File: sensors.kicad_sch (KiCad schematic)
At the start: 28 parts, among them IC1 TCA9548ARGERQ1, IC4 SGP40-D-R4, IC5 SGP40-D-R4, U2 BMP581, U4 BMP581

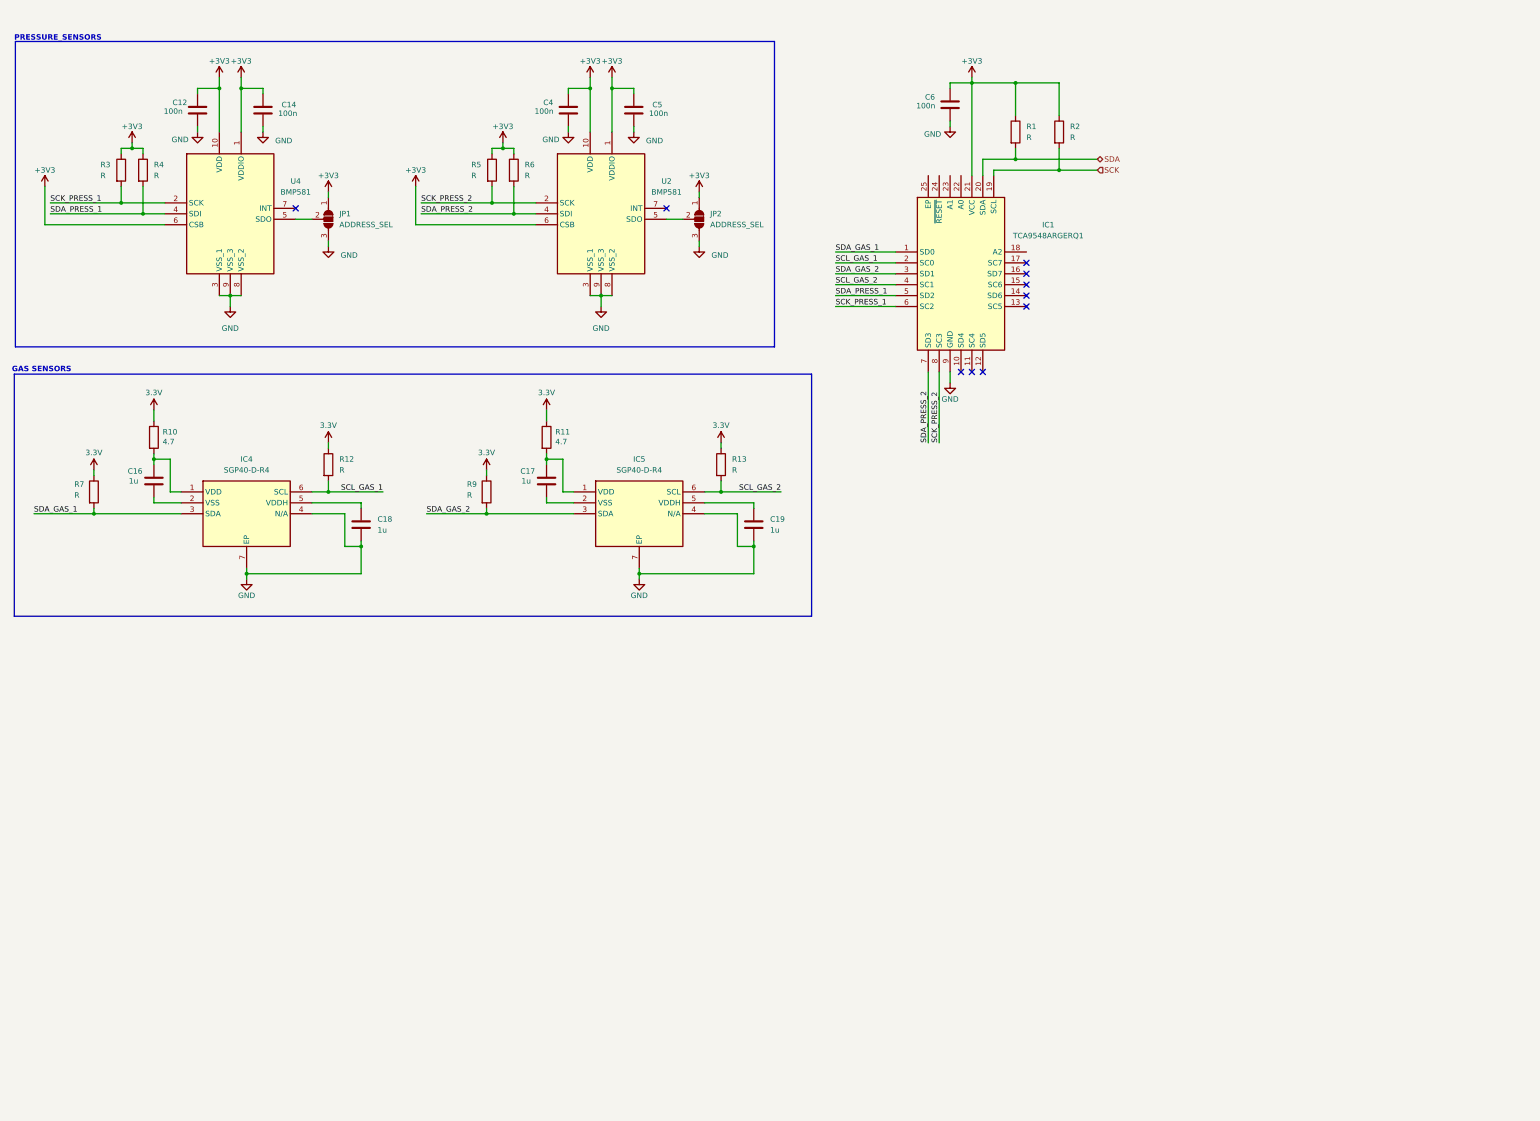
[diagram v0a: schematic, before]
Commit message: fix: arrange board for a total of 8 sensors, 4 DNP
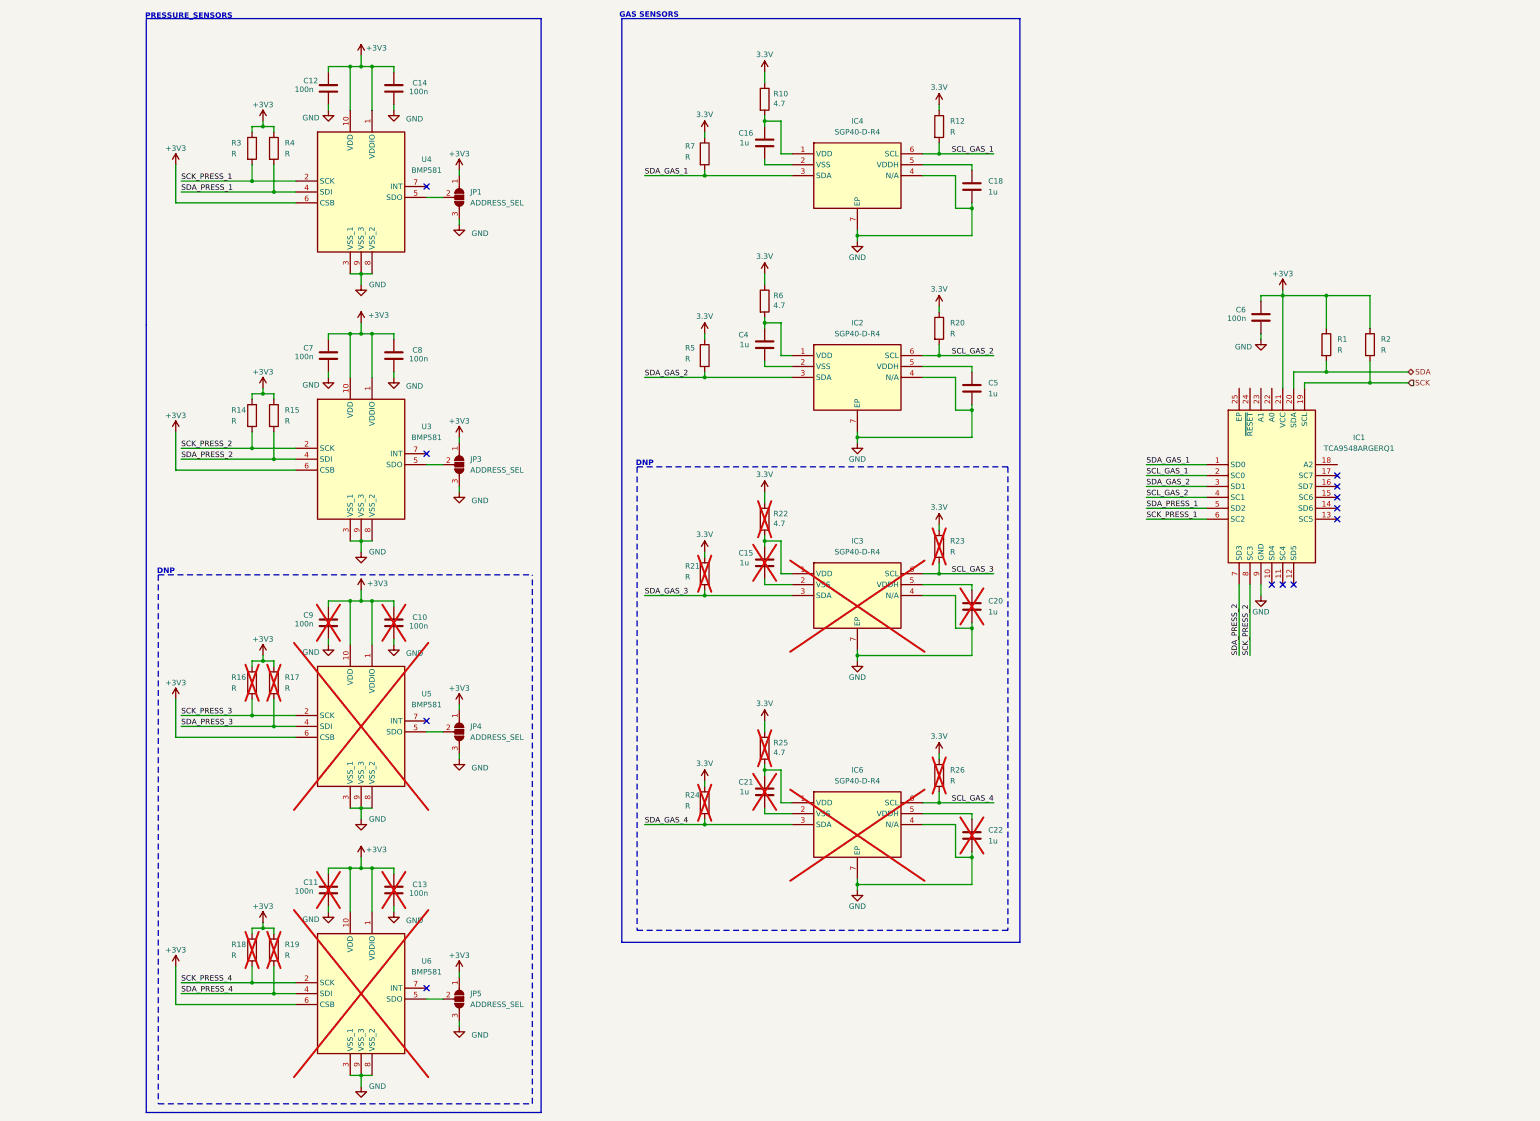
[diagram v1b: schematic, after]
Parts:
- removed C17, C19: 1u, symbol Device:C
- removed IC5: SGP40-D-R4, SON80P244X244X95-7N, symbol SGP40:SGP40-D-R4
- removed JP2: ADDRESS_SEL, symbol Jumper:SolderJumper_3_Open
- removed R11: 4.7, symbol Device:R
- removed R13, R9: R, symbol Device:R
- removed U2: BMP581, BMP581, symbol BMP581:BMP581
- added C10, C11, C13, C7, C8, C9: 100n, symbol Device:C
- added C15, C20, C21, C22: 1u, symbol Device:C
- added IC2, IC3, IC6: SGP40-D-R4, SON80P244X244X95-7N, symbol SGP40:SGP40-D-R4
- added JP3, JP4, JP5: ADDRESS_SEL, symbol Jumper:SolderJumper_3_Open
- added R14, R15, R16, R17, R18, R19, R20, R21, R23, R24, R26: R, symbol Device:R
- added R22, R25: 4.7, symbol Device:R
- added U3, U5, U6: BMP581, BMP581, symbol BMP581:BMP581
- C4, C5: value 100n -> 1u
- R6: value R -> 4.7
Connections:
- net +3V3: now also C10.1, C11.1, C13.1, C7.1, C8.1, C9.1, JP3.1 (A), JP4.1 (A), JP5.1 (A), R14.1, R15.1, R16.1, R17.1, R18.1, R19.1, U3.1 (VDDIO), U3.10 (VDD), U3.6 (CSB), U5.1 (VDDIO), U5.10 (VDD), U5.6 (CSB), U6.1 (VDDIO), U6.10 (VDD), U6.6 (CSB); no longer C4.1, C5.1, R5.1, R6.1
- net 3.3V: now also R5.1, R6.1, R20.1, R21.1, R22.1, R23.1, R24.1, R25.1, R26.1
- net GND: now also C10.2, C11.2, C13.2, C20.2, C22.2, C7.2, C8.2, C9.2, IC2.4 (N/A), IC2.7 (EP), IC3.4 (N/A), IC3.7 (EP), IC6.4 (N/A), IC6.7 (EP), JP3.3 (B), JP4.3 (B), JP5.3 (B), U3.3 (VSS_1), U3.8 (VSS_2), U3.9 (VSS_3), U5.3 (VSS_1), U5.8 (VSS_2), U5.9 (VSS_3), U6.3 (VSS_1), U6.8 (VSS_2), U6.9 (VSS_3); no longer C4.2
- net SCK_PRESS_2: now also R14.2, U3.2 (SCK); no longer R5.2
- net SCL_GAS_2: now also IC2.6 (SCL), R20.2
- net SDA_GAS_2: now also R5.2, IC2.3 (SDA)
- net SDA_PRESS_2: now also R15.2, U3.4 (SDI); no longer R6.2
- new net: JP4.2 (C), U5.5 (SDO)
- new net: C15.1, IC3.1 (VDD), R22.2
- new net: C15.2, IC3.2 (VSS)
- new net: C4.1, IC2.1 (VDD), R6.2
- new net: C5.1, IC2.5 (VDDH)
- new net: C4.2, IC2.2 (VSS)
- new net: C20.1, IC3.5 (VDDH)
- new net: C22.1, IC6.5 (VDDH)
- new net: JP5.2 (C), U6.5 (SDO)
- new net: JP3.2 (C), U3.5 (SDO)
- new net: C21.1, IC6.1 (VDD), R25.2
- new net: C21.2, IC6.2 (VSS)
- new net SCK_PRESS_3: R16.2, U5.2 (SCK)
- new net SCK_PRESS_4: R18.2, U6.2 (SCK)
- new net SCL_GAS_3: IC3.6 (SCL), R23.2
- new net SCL_GAS_4: IC6.6 (SCL), R26.2
- new net SDA_GAS_3: IC3.3 (SDA), R21.2
- new net SDA_GAS_4: IC6.3 (SDA), R24.2
- new net SDA_PRESS_3: R17.2, U5.4 (SDI)
- new net SDA_PRESS_4: R19.2, U6.4 (SDI)
- no-connect marks 10 -> 12
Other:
- note added: "DNP"
- moved on the sheet: C12, C14, C16, C18, C6, IC1, IC4, JP1, R1, R10, R12, R2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

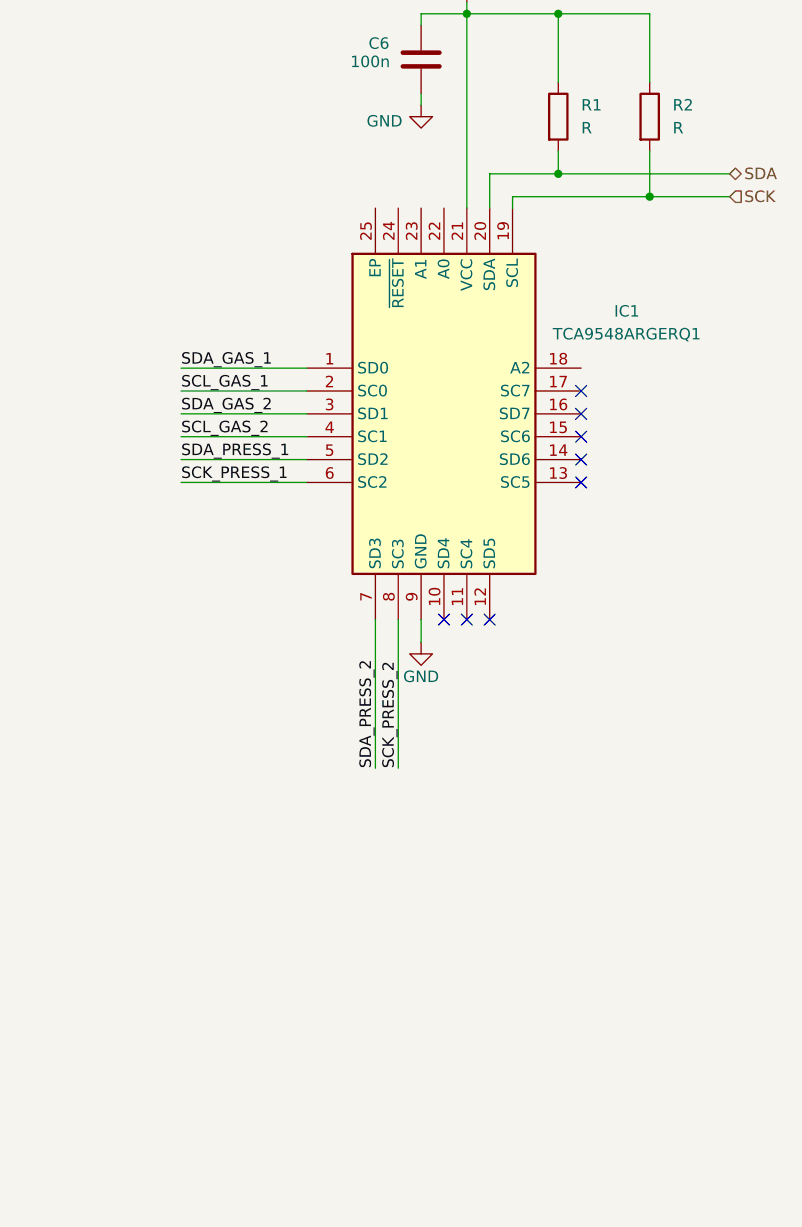
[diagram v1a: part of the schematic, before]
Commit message: feat: address selection i2c switch
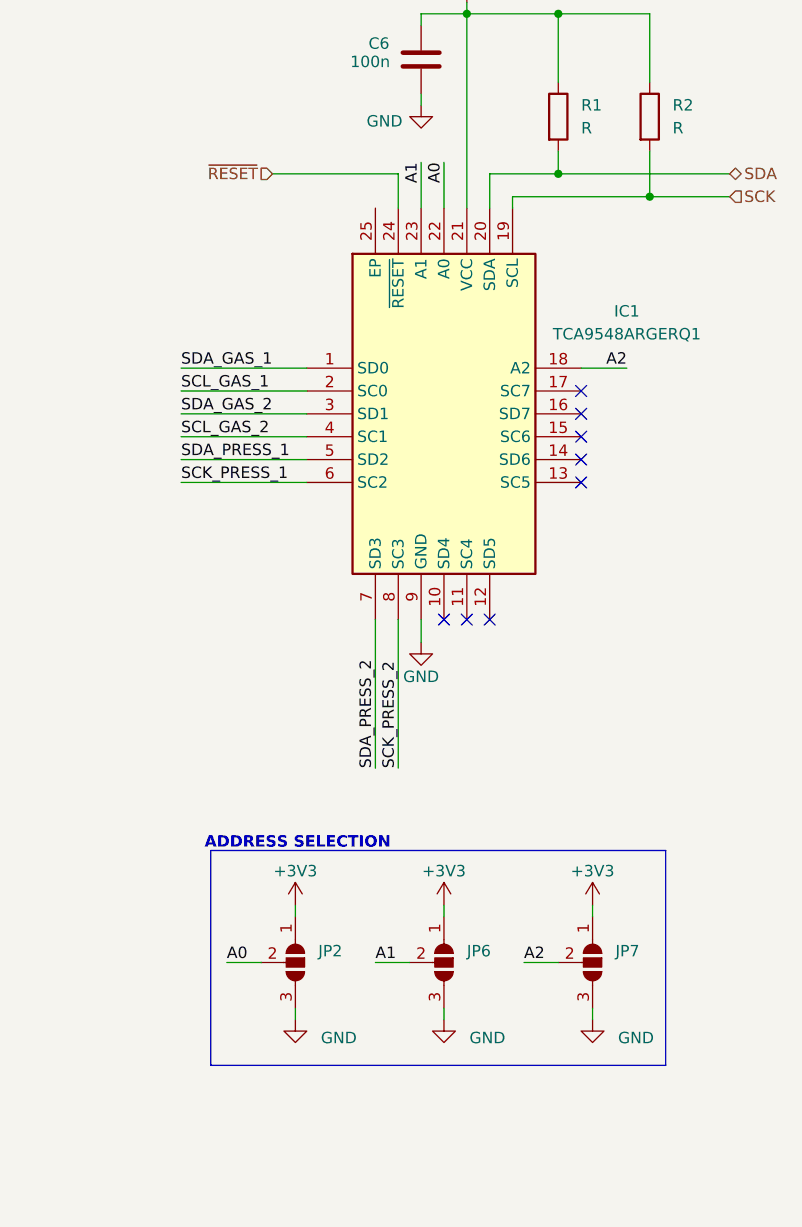
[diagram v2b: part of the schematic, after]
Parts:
- added JP2, JP6, JP7: SolderJumper_3_Open, symbol Jumper:SolderJumper_3_Open
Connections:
- net +3V3: now also JP2.1 (A), JP6.1 (A), JP7.1 (A)
- net GND: now also JP2.3 (B), JP6.3 (B), JP7.3 (B)
- net A2: now reaches IC1.18 (A2)
- net A2: now also JP7.2 (C)
- net A0: now reaches IC1.22 (A0)
- net A0: now also JP2.2 (C)
- net A1: now reaches IC1.23 (A1)
- net A1: now also JP6.2 (C)
- net ~{RESET}: now reaches IC1.24 (~{RESET})
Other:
- note added: "ADDRESS SELECTION"

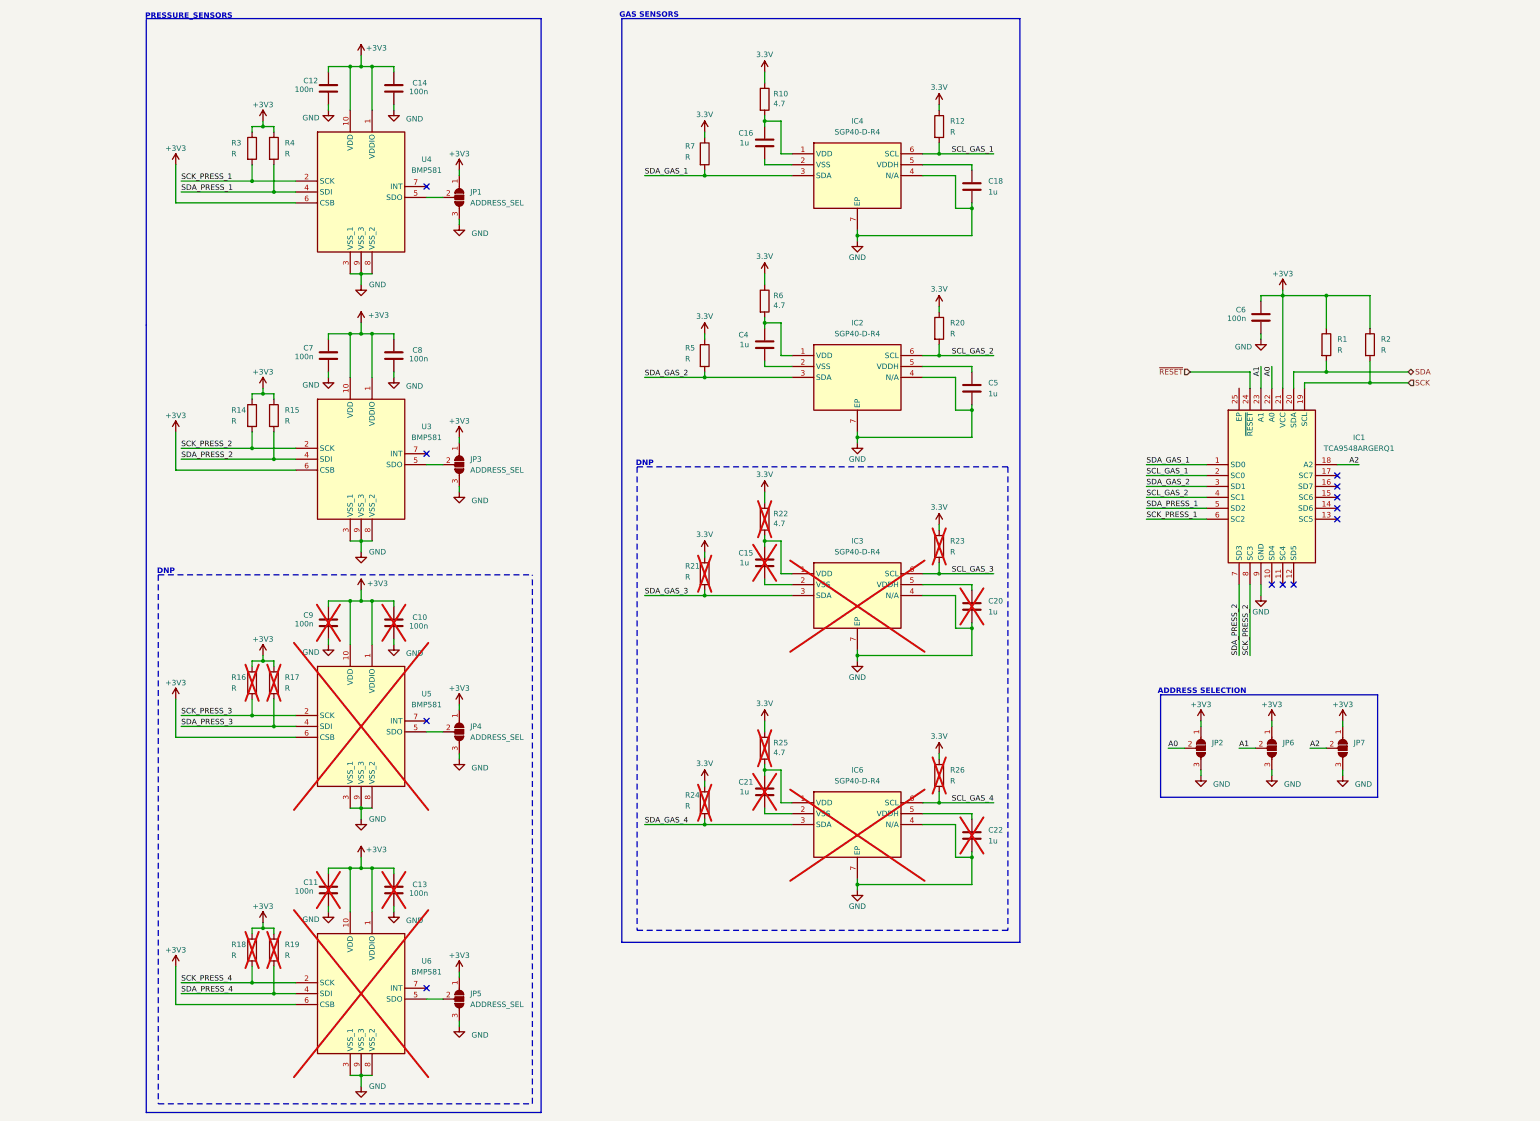
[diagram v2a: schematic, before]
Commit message: feat: rasp connections + fan
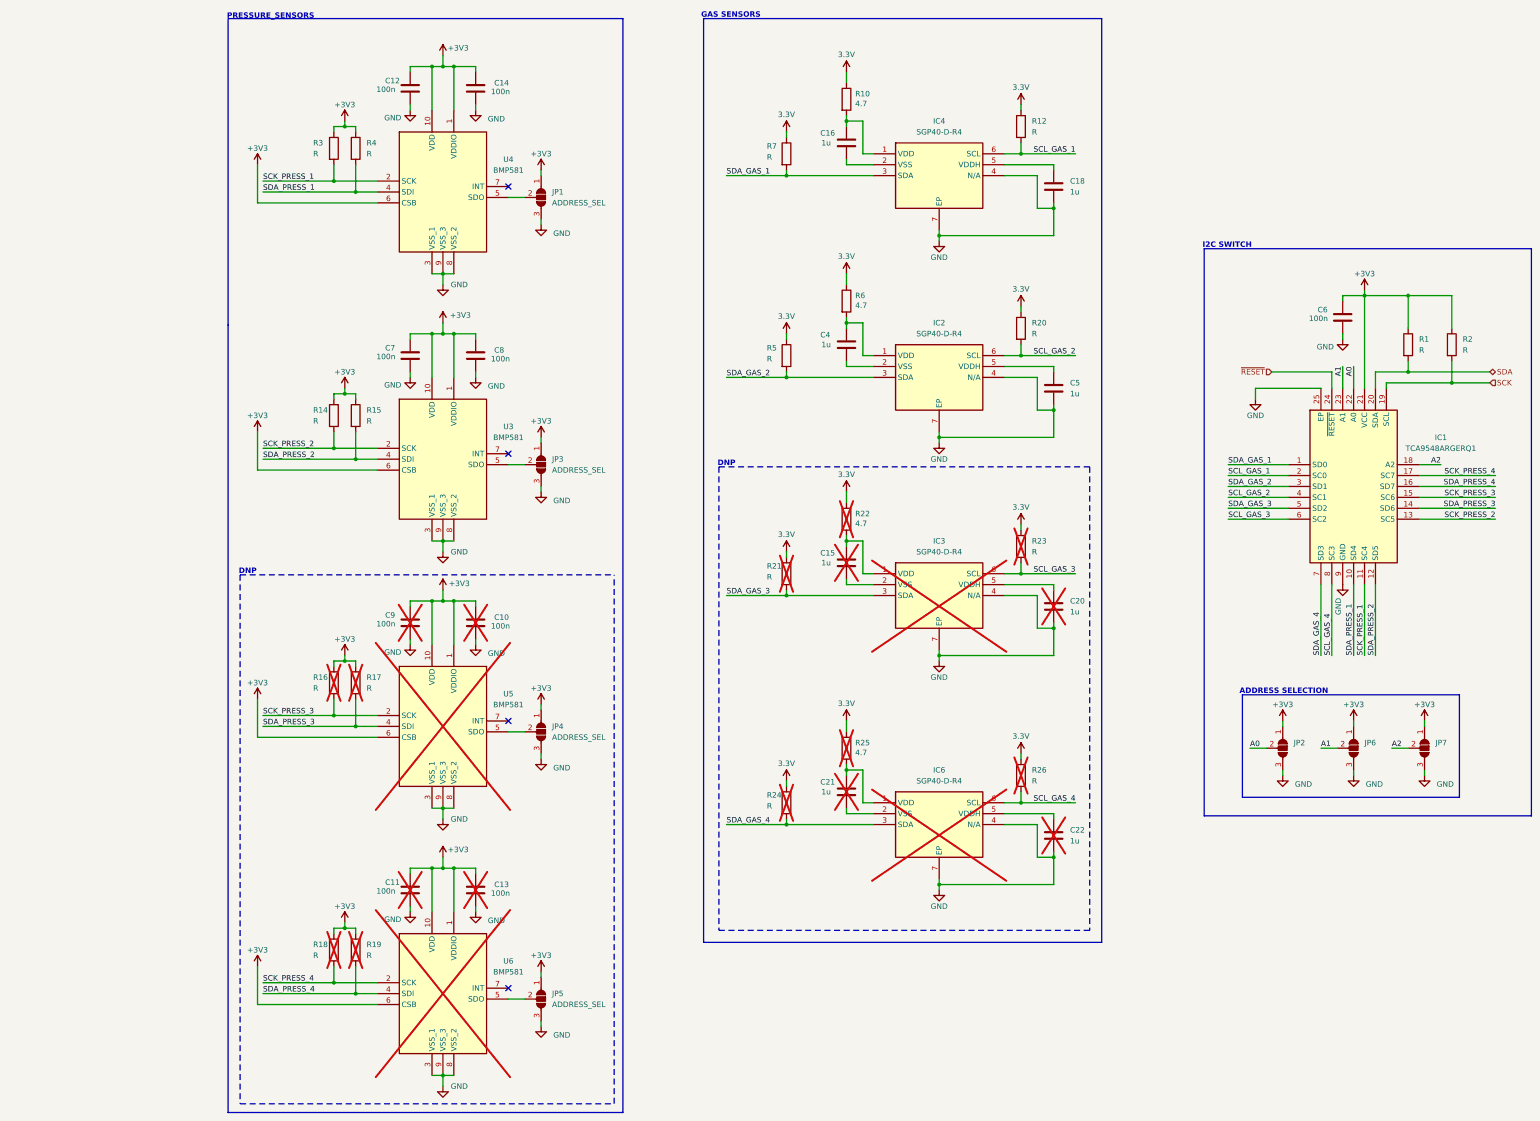
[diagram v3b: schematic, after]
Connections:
- net GND: now also IC1.25 (EP)
- net SCK_PRESS_1: now also IC1.11 (SC4); no longer IC1.6 (SC2)
- net SCK_PRESS_2: now also IC1.13 (SC5); no longer IC1.8 (SC3)
- net SCK_PRESS_3: now also IC1.15 (SC6)
- net SCK_PRESS_4: now also IC1.17 (SC7)
- net SCL_GAS_3: now also IC1.6 (SC2)
- net SCL_GAS_4: now also IC1.8 (SC3)
- net SDA_GAS_3: now also IC1.5 (SD2)
- net SDA_GAS_4: now also IC1.7 (SD3)
- net SDA_PRESS_1: now also IC1.10 (SD4); no longer IC1.5 (SD2)
- net SDA_PRESS_2: now also IC1.12 (SD5); no longer IC1.7 (SD3)
- net SDA_PRESS_3: now also IC1.14 (SD6)
- net SDA_PRESS_4: now also IC1.16 (SD7)
- no-connect marks 12 -> 4
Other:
- note added: "I2C SWITCH"
- moved on the sheet: C10, C11, C12, C13, C14, C15, C16, C18, C20, C21, C22, C4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
